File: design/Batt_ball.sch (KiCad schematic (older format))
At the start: 6 parts

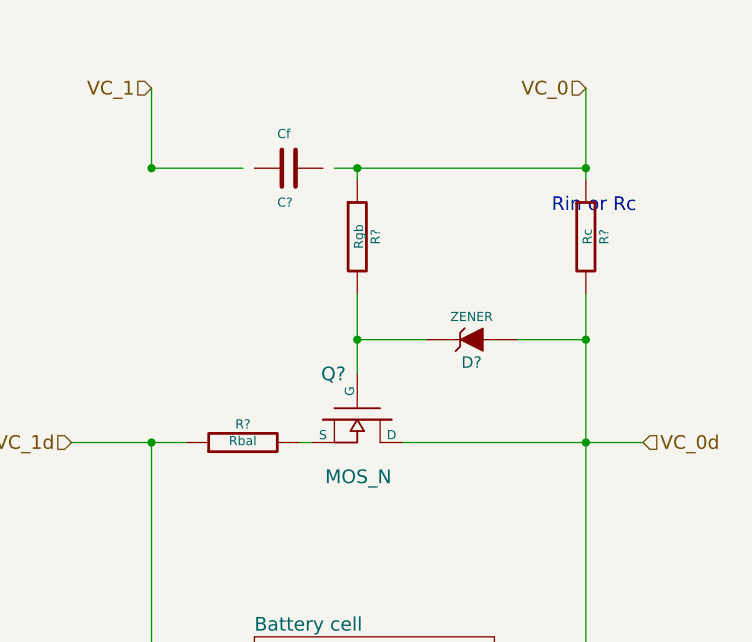
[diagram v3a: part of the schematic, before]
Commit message: Add new example in datasheet define more values
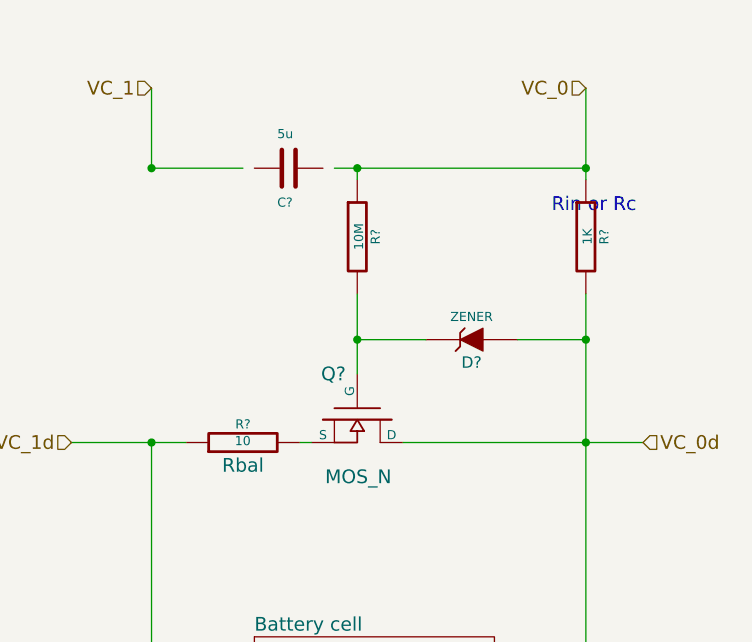
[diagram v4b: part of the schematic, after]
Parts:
- C?: value Cf -> 5u; Name (none) -> Cc
- R?: value Rbal -> 10; Name (none) -> Rbal
- R?: value Rc -> 1K
- R?: value Rgb -> 10M
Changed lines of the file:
@@
 $Descr A4 11693 8268
 encoding utf-8
-Sheet 35 101
+Sheet 6 101
 Title ""
 Date ""
@@
 AR Path="/3A58CB36/3A539FA4/55BD5928" Ref="R?"  Part="1"
 F 0 "R?" V 4980 2850 40  0000 C CNN
-F 1 "Rbal" V 4907 2851 40  0000 C CNN
+F 1 "10" V 4907 2851 40  0000 C CNN
 F 2 "" V 4830 2850 30  0000 C CNN
 F 3 "" H 4900 2850 30  0000 C CNN
+F 4 "Rbal" V 4800 2850 60  0000 C CNN "Name"
 	1    4900 2850
 	0    -1   -1   0
@@
 AR Path="/3A58CB36/3A539FA4/55BD5B30" Ref="R?"  Part="1"
 F 0 "R?" V 6480 1950 40  0000 C CNN
-F 1 "Rc" V 6407 1951 40  0000 C CNN
+F 1 "1K" V 6407 1951 40  0000 C CNN
 F 2 "" V 6330 1950 30  0000 C CNN
 F 3 "" H 6400 1950 30  0000 C CNN
@@
 AR Path="/3A58CB36/3A539FA4/55BD5F3E" Ref="C?"  Part="1"
 F 0 "C?" V 5250 1600 40  0000 L CNN
-F 1 "Cf" V 4950 1600 40  0000 L CNN
+F 1 "5u" V 4950 1600 40  0000 L CNN
 F 2 "" H 5138 1500 30  0000 C CNN
 F 3 "" H 5100 1650 60  0000 C CNN
+F 4 "Cc" V 5100 1650 60  0001 C CNN "Name"
 	1    5100 1650
 	0    1    1    0
@@
 AR Path="/3A58CB36/3A539FA4/55BD60D7" Ref="R?"  Part="1"
 F 0 "R?" V 5480 1950 40  0000 C CNN
-F 1 "Rgb" V 5407 1951 40  0000 C CNN
+F 1 "10M" V 5407 1951 40  0000 C CNN
 F 2 "" V 5330 1950 30  0000 C CNN
 F 3 "" H 5400 1950 30  0000 C CNN

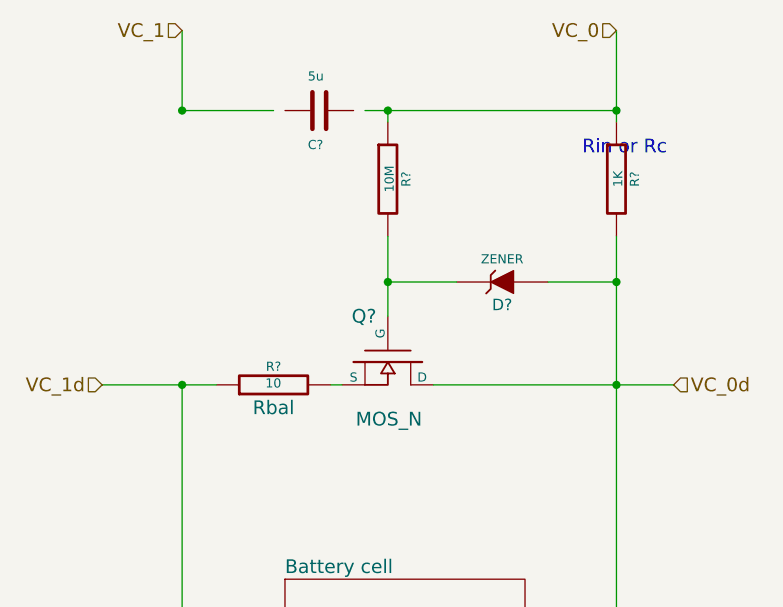
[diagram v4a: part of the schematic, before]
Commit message: Fix some schematic update pdf
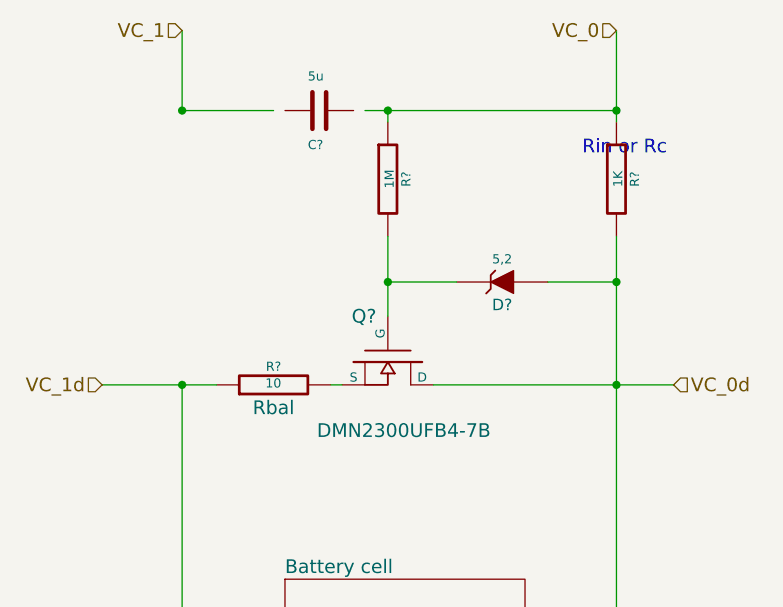
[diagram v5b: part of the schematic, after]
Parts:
- D?: value ZENER -> 5,2
- Q?: value MOS_N -> DMN2300UFB4-7B
- R?: value 10M -> 1M
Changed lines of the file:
@@
 $Descr A4 11693 8268
 encoding utf-8
-Sheet 6 101
+Sheet 14 101
 Title ""
 Date ""
@@
 AR Path="/3A58CB36/3A5364FA/55BD57AA" Ref="Q?"  Part="1"
 AR Path="/3A58CB36/3A539FA4/55BD57AA" Ref="Q?"  Part="1"
+AR Path="/55C14E4B/3A5B5476/3A501D31/55BD57AA" Ref="Q?"  Part="1"
+AR Path="/55C14E4B/3A5B5476/3A5031D0/55BD57AA" Ref="Q?"  Part="1"
+AR Path="/55C14E4B/3A5B5476/3A507C61/55BD57AA" Ref="Q?"  Part="1"
+AR Path="/55C14E4B/3A5B5476/3A509CE9/55BD57AA" Ref="Q?"  Part="1"
+AR Path="/55C14E4B/3A5B5476/3A53CBC8/55BD57AA" Ref="Q?"  Part="1"
+AR Path="/55C14E4B/3A5B5476/3A5401FD/55BD57AA" Ref="Q?"  Part="1"
+AR Path="/55C14E4B/3A5B5476/3A5314A2/55BD57AA" Ref="Q?"  Part="1"
+AR Path="/55C14E4B/3A5B5476/3A5364FA/55BD57AA" Ref="Q?"  Part="1"
+AR Path="/55C14E4B/3A5B5476/3A539FA4/55BD57AA" Ref="Q?"  Part="1"
 F 0 "Q?" V 5200 2700 60  0000 R CNN
-F 1 "MOS_N" V 5650 2900 60  0000 R CNN
+F 1 "DMN2300UFB4-7B" V 5700 3200 60  0000 R CNN
 F 2 "" H 5400 2750 60  0000 C CNN
 F 3 "" H 5400 2750 60  0000 C CNN
@@
 AR Path="/3A58CB36/3A5364FA/55BD5928" Ref="R?"  Part="1"
 AR Path="/3A58CB36/3A539FA4/55BD5928" Ref="R?"  Part="1"
+AR Path="/55C14E4B/3A5B5476/3A501D31/55BD5928" Ref="R?"  Part="1"
+AR Path="/55C14E4B/3A5B5476/3A5031D0/55BD5928" Ref="R?"  Part="1"
+AR Path="/55C14E4B/3A5B5476/3A507C61/55BD5928" Ref="R?"  Part="1"
+AR Path="/55C14E4B/3A5B5476/3A509CE9/55BD5928" Ref="R?"  Part="1"
+AR Path="/55C14E4B/3A5B5476/3A53CBC8/55BD5928" Ref="R?"  Part="1"
+AR Path="/55C14E4B/3A5B5476/3A5401FD/55BD5928" Ref="R?"  Part="1"
+AR Path="/55C14E4B/3A5B5476/3A5314A2/55BD5928" Ref="R?"  Part="1"
+AR Path="/55C14E4B/3A5B5476/3A5364FA/55BD5928" Ref="R?"  Part="1"
+AR Path="/55C14E4B/3A5B5476/3A539FA4/55BD5928" Ref="R?"  Part="1"
 F 0 "R?" V 4980 2850 40  0000 C CNN
 F 1 "10" V 4907 2851 40  0000 C CNN
@@
 AR Path="/3A58CB36/3A5364FA/55BD5ABC" Ref="D?"  Part="1"
 AR Path="/3A58CB36/3A539FA4/55BD5ABC" Ref="D?"  Part="1"
+AR Path="/55C14E4B/3A5B5476/3A501D31/55BD5ABC" Ref="D?"  Part="1"
+AR Path="/55C14E4B/3A5B5476/3A5031D0/55BD5ABC" Ref="D?"  Part="1"
+AR Path="/55C14E4B/3A5B5476/3A507C61/55BD5ABC" Ref="D?"  Part="1"
+AR Path="/55C14E4B/3A5B5476/3A509CE9/55BD5ABC" Ref="D?"  Part="1"
+AR Path="/55C14E4B/3A5B5476/3A53CBC8/55BD5ABC" Ref="D?"  Part="1"
+AR Path="/55C14E4B/3A5B5476/3A5401FD/55BD5ABC" Ref="D?"  Part="1"
+AR Path="/55C14E4B/3A5B5476/3A5314A2/55BD5ABC" Ref="D?"  Part="1"
+AR Path="/55C14E4B/3A5B5476/3A5364FA/55BD5ABC" Ref="D?"  Part="1"
+AR Path="/55C14E4B/3A5B5476/3A539FA4/55BD5ABC" Ref="D?"  Part="1"
 F 0 "D?" H 5900 2500 50  0000 C CNN
-F 1 "ZENER" H 5900 2300 40  0000 C CNN
+F 1 "5,2" H 5900 2300 40  0000 C CNN
 F 2 "" H 5900 2400 60  0000 C CNN
 F 3 "" H 5900 2400 60  0000 C CNN
@@
 AR Path="/3A58CB36/3A5364FA/55BD5B30" Ref="R?"  Part="1"
 AR Path="/3A58CB36/3A539FA4/55BD5B30" Ref="R?"  Part="1"
+AR Path="/55C14E4B/3A5B5476/3A501D31/55BD5B30" Ref="R?"  Part="1"
+AR Path="/55C14E4B/3A5B5476/3A5031D0/55BD5B30" Ref="R?"  Part="1"
+AR Path="/55C14E4B/3A5B5476/3A507C61/55BD5B30" Ref="R?"  Part="1"
+AR Path="/55C14E4B/3A5B5476/3A509CE9/55BD5B30" Ref="R?"  Part="1"
+AR Path="/55C14E4B/3A5B5476/3A53CBC8/55BD5B30" Ref="R?"  Part="1"
+AR Path="/55C14E4B/3A5B5476/3A5401FD/55BD5B30" Ref="R?"  Part="1"
+AR Path="/55C14E4B/3A5B5476/3A5314A2/55BD5B30" Ref="R?"  Part="1"
+AR Path="/55C14E4B/3A5B5476/3A5364FA/55BD5B30" Ref="R?"  Part="1"
+AR Path="/55C14E4B/3A5B5476/3A539FA4/55BD5B30" Ref="R?"  Part="1"
 F 0 "R?" V 6480 1950 40  0000 C CNN
 F 1 "1K" V 6407 1951 40  0000 C CNN
@@
 AR Path="/3A58CB36/3A5364FA/55BD5F3E" Ref="C?"  Part="1"
 AR Path="/3A58CB36/3A539FA4/55BD5F3E" Ref="C?"  Part="1"
+AR Path="/55C14E4B/3A5B5476/3A501D31/55BD5F3E" Ref="C?"  Part="1"
+AR Path="/55C14E4B/3A5B5476/3A5031D0/55BD5F3E" Ref="C?"  Part="1"
+AR Path="/55C14E4B/3A5B5476/3A507C61/55BD5F3E" Ref="C?"  Part="1"
+AR Path="/55C14E4B/3A5B5476/3A509CE9/55BD5F3E" Ref="C?"  Part="1"
+AR Path="/55C14E4B/3A5B5476/3A53CBC8/55BD5F3E" Ref="C?"  Part="1"
+AR Path="/55C14E4B/3A5B5476/3A5401FD/55BD5F3E" Ref="C?"  Part="1"
+AR Path="/55C14E4B/3A5B5476/3A5314A2/55BD5F3E" Ref="C?"  Part="1"
+AR Path="/55C14E4B/3A5B5476/3A5364FA/55BD5F3E" Ref="C?"  Part="1"
+AR Path="/55C14E4B/3A5B5476/3A539FA4/55BD5F3E" Ref="C?"  Part="1"
 F 0 "C?" V 5250 1600 40  0000 L CNN
 F 1 "5u" V 4950 1600 40  0000 L CNN
@@
 AR Path="/3A58CB36/3A5364FA/55BD60D7" Ref="R?"  Part="1"
 AR Path="/3A58CB36/3A539FA4/55BD60D7" Ref="R?"  Part="1"
+AR Path="/55C14E4B/3A5B5476/3A501D31/55BD60D7" Ref="R?"  Part="1"
+AR Path="/55C14E4B/3A5B5476/3A5031D0/55BD60D7" Ref="R?"  Part="1"
+AR Path="/55C14E4B/3A5B5476/3A507C61/55BD60D7" Ref="R?"  Part="1"
+AR Path="/55C14E4B/3A5B5476/3A509CE9/55BD60D7" Ref="R?"  Part="1"
+AR Path="/55C14E4B/3A5B5476/3A53CBC8/55BD60D7" Ref="R?"  Part="1"
+AR Path="/55C14E4B/3A5B5476/3A5401FD/55BD60D7" Ref="R?"  Part="1"
+AR Path="/55C14E4B/3A5B5476/3A5314A2/55BD60D7" Ref="R?"  Part="1"
+AR Path="/55C14E4B/3A5B5476/3A5364FA/55BD60D7" Ref="R?"  Part="1"
+AR Path="/55C14E4B/3A5B5476/3A539FA4/55BD60D7" Ref="R?"  Part="1"
 F 0 "R?" V 5480 1950 40  0000 C CNN
-F 1 "10M" V 5407 1951 40  0000 C CNN
+F 1 "1M" V 5407 1951 40  0000 C CNN
 F 2 "" V 5330 1950 30  0000 C CNN
 F 3 "" H 5400 1950 30  0000 C CNN

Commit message: Add a new BQ and start routing board for (reason for separation for easier routing) but in the end I souldnt do this becasue of netlist but its ok because of symlink
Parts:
- removed Q?: DMN2300UFB4-7B, symbol MOS_N
- added Q?: MOSFET_N, symbol MOSFET_N
- C?: value 5u -> 10u; symbol C -> C-RESCUE-BMS
- D?: value 5,2 -> 5,6; symbol ZENER -> ZENER-RESCUE-BMS
- R?: value 10 -> 50; symbol R -> R-RESCUE-BMS
- R?: symbol R -> R-RESCUE-BMS
- R?: value 1M -> 10K; symbol R -> R-RESCUE-BMS
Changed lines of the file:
@@
 EESchema Schematic File Version 2
+LIBS:BMS-rescue
 LIBS:iso5500
 LIBS:crf_1
@@
 $Descr A4 11693 8268
 encoding utf-8
-Sheet 97 101
+Sheet 32 101
 Title ""
 Date ""
@@
 This is just mesurment and balancing circuit
 $Comp
-L MOS_N Q?
-U 1 1 55BD57AA
-P 5400 2750
-AR Path="/55BB8FBC/3A501D31/55BD57AA" Ref="Q?"  Part="1"
-AR Path="/55BB8FBC/3A507C61/55BD57AA" Ref="Q?"  Part="1"
-AR Path="/55BB8FBC/3A509CE9/55BD57AA" Ref="Q?"  Part="1"
-AR Path="/55BB8FBC/3A53CBC8/55BD57AA" Ref="Q?"  Part="1"
-AR Path="/55BB8FBC/3A539FA4/55BD57AA" Ref="Q?"  Part="1"
-AR Path="/55BB8FBC/3A5B5476/3A501D31/55BD57AA" Ref="Q?"  Part="1"
-AR Path="/55BB8FBC/3A5B5476/3A5031D0/55BD57AA" Ref="Q?"  Part="1"
-AR Path="/55BB8FBC/3A5B5476/3A507C61/55BD57AA" Ref="Q?"  Part="1"
-AR Path="/55BB8FBC/3A5B5476/3A509CE9/55BD57AA" Ref="Q?"  Part="1"
-AR Path="/55BB8FBC/3A5B5476/3A53CBC8/55BD57AA" Ref="Q?"  Part="1"
-AR Path="/55BB8FBC/3A5B5476/3A5401FD/55BD57AA" Ref="Q?"  Part="1"
-AR Path="/55BB8FBC/3A5B5476/3A5314A2/55BD57AA" Ref="Q?"  Part="1"
-AR Path="/55BB8FBC/3A5B5476/3A5364FA/55BD57AA" Ref="Q?"  Part="1"
-AR Path="/55BB8FBC/3A5B5476/3A539FA4/55BD57AA" Ref="Q?"  Part="1"
-AR Path="/3A58CB36/3A501D31/55BD57AA" Ref="Q?"  Part="1"
-AR Path="/3A58CB36/3A5031D0/55BD57AA" Ref="Q?"  Part="1"
-AR Path="/3A58CB36/3A507C61/55BD57AA" Ref="Q?"  Part="1"
-AR Path="/3A58CB36/3A509CE9/55BD57AA" Ref="Q?"  Part="1"
-AR Path="/3A58CB36/3A53CBC8/55BD57AA" Ref="Q?"  Part="1"
-AR Path="/3A58CB36/3A5401FD/55BD57AA" Ref="Q?"  Part="1"
-AR Path="/3A58CB36/3A5314A2/55BD57AA" Ref="Q?"  Part="1"
-AR Path="/3A58CB36/3A5364FA/55BD57AA" Ref="Q?"  Part="1"
-AR Path="/3A58CB36/3A539FA4/55BD57AA" Ref="Q?"  Part="1"
-AR Path="/55C14E4B/3A5B5476/3A501D31/55BD57AA" Ref="Q?"  Part="1"
-AR Path="/55C14E4B/3A5B5476/3A5031D0/55BD57AA" Ref="Q?"  Part="1"
-AR Path="/55C14E4B/3A5B5476/3A507C61/55BD57AA" Ref="Q?"  Part="1"
-AR Path="/55C14E4B/3A5B5476/3A509CE9/55BD57AA" Ref="Q?"  Part="1"
-AR Path="/55C14E4B/3A5B5476/3A53CBC8/55BD57AA" Ref="Q?"  Part="1"
-AR Path="/55C14E4B/3A5B5476/3A5401FD/55BD57AA" Ref="Q?"  Part="1"
-AR Path="/55C14E4B/3A5B5476/3A5314A2/55BD57AA" Ref="Q?"  Part="1"
-AR Path="/55C14E4B/3A5B5476/3A5364FA/55BD57AA" Ref="Q?"  Part="1"
-AR Path="/55C14E4B/3A5B5476/3A539FA4/55BD57AA" Ref="Q?"  Part="1"
-F 0 "Q?" V 5200 2700 60  0000 R CNN
-F 1 "DMN2300UFB4-7B" V 5700 3200 60  0000 R CNN
-F 2 "" H 5400 2750 60  0000 C CNN
-F 3 "" H 5400 2750 60  0000 C CNN
-	1    5400 2750
-	0    1    1    0
-$EndComp
-$Comp
-L R R?
+L R-RESCUE-BMS R?
 U 1 1 55BD5928
 P 4900 2850
@@
 AR Path="/55C14E4B/3A5B5476/3A5364FA/55BD5928" Ref="R?"  Part="1"
 AR Path="/55C14E4B/3A5B5476/3A539FA4/55BD5928" Ref="R?"  Part="1"
+AR Path="/55BD5928" Ref="R?"  Part="1"
 F 0 "R?" V 4980 2850 40  0000 C CNN
-F 1 "10" V 4907 2851 40  0000 C CNN
+F 1 "50" V 4907 2851 40  0000 C CNN
 F 2 "" V 4830 2850 30  0000 C CNN
 F 3 "" H 4900 2850 30  0000 C CNN
@@
 $EndComp
 $Comp
-L ZENER D?
+L ZENER-RESCUE-BMS D?
 U 1 1 55BD5ABC
 P 5900 2400
@@
 AR Path="/55C14E4B/3A5B5476/3A539FA4/55BD5ABC" Ref="D?"  Part="1"
 F 0 "D?" H 5900 2500 50  0000 C CNN
-F 1 "5,2" H 5900 2300 40  0000 C CNN
+F 1 "5,6" H 5900 2300 40  0000 C CNN
 F 2 "" H 5900 2400 60  0000 C CNN
 F 3 "" H 5900 2400 60  0000 C CNN
@@
 $EndComp
 $Comp
-L R R?
+L R-RESCUE-BMS R?
 U 1 1 55BD5B30
 P 6400 1950
@@
 AR Path="/55C14E4B/3A5B5476/3A5364FA/55BD5B30" Ref="R?"  Part="1"
 AR Path="/55C14E4B/3A5B5476/3A539FA4/55BD5B30" Ref="R?"  Part="1"
+AR Path="/55BD5B30" Ref="R?"  Part="1"
 F 0 "R?" V 6480 1950 40  0000 C CNN
 F 1 "1K" V 6407 1951 40  0000 C CNN
@@
 $EndComp
 $Comp
-L C C?
+L C-RESCUE-BMS C?
 U 1 1 55BD5F3E
 P 5100 1650
@@
 AR Path="/55C14E4B/3A5B5476/3A5364FA/55BD5F3E" Ref="C?"  Part="1"
 AR Path="/55C14E4B/3A5B5476/3A539FA4/55BD5F3E" Ref="C?"  Part="1"
+AR Path="/55BD5F3E" Ref="C?"  Part="1"
 F 0 "C?" V 5250 1600 40  0000 L CNN
-F 1 "5u" V 4950 1600 40  0000 L CNN
+F 1 "10u" V 4950 1600 40  0000 L CNN
 F 2 "" H 5138 1500 30  0000 C CNN
 F 3 "" H 5100 1650 60  0000 C CNN
@@
 	4500 1650 4900 1650
 $Comp
-L R R?
+L R-RESCUE-BMS R?
 U 1 1 55BD60D7
 P 5400 1950
@@
 AR Path="/55C14E4B/3A5B5476/3A5364FA/55BD60D7" Ref="R?"  Part="1"
 AR Path="/55C14E4B/3A5B5476/3A539FA4/55BD60D7" Ref="R?"  Part="1"
+AR Path="/55BD60D7" Ref="R?"  Part="1"
 F 0 "R?" V 5480 1950 40  0000 C CNN
-F 1 "1M" V 5407 1951 40  0000 C CNN
+F 1 "10K" V 5407 1951 40  0000 C CNN
 F 2 "" V 5330 1950 30  0000 C CNN
 F 3 "" H 5400 1950 30  0000 C CNN
@@
 Wire Wire Line
 	4500 1650 4500 1300
+$Comp
+L MOSFET_N Q?
+U 1 1 565A36F5
+P 5400 2750
+F 0 "Q?" H 5410 2920 60  0000 R CNN
+F 1 "MOSFET_N" H 5410 2600 60  0000 R CNN
+F 2 "" H 5400 2750 60  0000 C CNN
+F 3 "" H 5400 2750 60  0000 C CNN
+	1    5400 2750
+	0    1    1    0
+$EndComp
 $EndSCHEMATC
